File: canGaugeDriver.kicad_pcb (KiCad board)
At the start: 2 copper layers, 74.7 x 41.4 mm, 40 parts, among them J1 CANbed 1.0 Interface, J2 VIN INTERFACE, J3 BLUESMIRF, J4 1848710, U1 TPL7407LA, U2 TPL7407LA

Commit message: fixed headers
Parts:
- removed J3: BLUESMIRF, Connector_PinHeader_2.54mm:PinHeader_1x06_P2.54mm_Vertical
- moved J2 8.23 mm to (149.3, 76.9), turned to 0 degrees
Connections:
- J1 pad 10: /D0_RX -> /D8_SEATBELT
- J1 pad 11: /D1_TX -> /A0
- J1 pad 12: /D2_SRS -> /D9_FUEL
- J1 pad 13: /D3_SPEED -> /A1
- J1 pad 14: /D8_SEATBELT -> /D10_OIL
- J1 pad 15: /D9_FUEL -> /A2
- J1 pad 16: /D10_OIL -> /D11_TACH
- J1 pad 17: /D11_TACH -> /5V
- J1 pad 2: /D5_COOL -> /D0_RX
- J1 pad 3: /D6_ABS -> /D5_COOL
- J1 pad 4: /A3 -> /D1_TX
- J1 pad 5: /D12_ALT -> /D6_ABS
- J1 pad 6: /A0 -> /D2_SRS
- J1 pad 7: /A1 -> /A3
- J1 pad 8: /A2 -> /D3_SPEED
- J1 pad 9: /5V -> /D12_ALT
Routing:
- net /D0_RX: track 28.7 -> 0.00 mm, vias 1 -> 0
- net /D1_TX: track 24.6 -> 0.00 mm, vias 1 -> 0
- net /D11_TACH: track 51.7 -> 38.8 mm
- net /D5_COOL: track 32.7 -> 19.9 mm
- net /VIN: track 99.3 -> 87.9 mm
- net /5V: track 53.5 -> 44.9 mm
- net /D6_ABS: track 37.2 -> 29.6 mm
- net /D12_ALT: track 46.1 -> 38.8 mm
- net /A0: track 12.9 -> 6.20 mm
- net /A1: track 15.3 -> 9.22 mm
- net /A3: track 40.6 -> 35.7 mm
- net /D8_SEATBELT: track 54.0 -> 50.4 mm
- net /D9_FUEL: track 57.6 -> 54.0 mm
- net /A2: track 20.5 -> 17.0 mm
- net /D2_SRS: track 49.7 -> 47.3 mm
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
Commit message: replaced output connector
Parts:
- removed J4: 1848710, PHOENIX_1848710:PHOENIX_1848710
- added J3: 348260240, MOLEX_348260240:CONN_SD-34826-001_24_MOL, F.Cu at (162.6, 93.6)
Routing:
- net /AI3: track 72.1 -> 43.9 mm
- net /AI2: track 67.8 -> 43.9 mm
- net /AI1: track 74.4 -> 52.5 mm
- net /D12_OUT: track 33.7 -> 13.3 mm
- net /D8_OUT: track 36.5 -> 17.0 mm, vias 2 -> 1
- net /D6_OUT: track 32.0 -> 14.3 mm
- net /D5_OUT: track 28.8 -> 13.9 mm
- net /AI0: track 23.4 -> 8.53 mm
- net /D9_OUT: track 42.6 -> 29.6 mm
- net /D11_OUT: track 26.5 -> 14.1 mm
- net /D4_OUT: track 26.4 -> 14.7 mm
- net /D10_OUT: track 27.9 -> 17.5 mm
- net /D3_OUT: track 26.4 -> 17.1 mm
- net /D2_OUT: track 25.3 -> 17.7 mm

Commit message: progress
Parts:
- removed the ? at (130.0, 73.9)
- added J4: DB9'MEAL', canGaugeDriver:DB9-MEAL, F.Cu at (147.8, 80.9)
- C1, C2, C3, C4, C5, C6, JP1, JP2, R1, R10, R11, R12, R13, R14, R15, R16, R17, R18, R19, R2, R20, R21, R3, R4, R5, R6, R7, R8, R9: moved to B.Cu
- moved R16 31.0 mm to (133.1, 74.8), turned to 0 degrees
- moved JP1 30.3 mm to (128.0, 91.1), turned to 180 degrees
- moved R21 28.1 mm to (127.5, 98.2), turned to 90 degrees
- moved R17 27.8 mm to (133.1, 77.1), turned to 0 degrees
- moved R13 27.7 mm to (133.1, 71.0), turned to 0 degrees
- moved R15 24.9 mm to (133.1, 69.0), turned to 0 degrees
- moved R18 24.8 mm to (133.1, 79.1), turned to 0 degrees
- moved R14 22.3 mm to (133.1, 67.2), turned to 0 degrees
- moved R19 21.5 mm to (118.6, 81.7), turned to 0 degrees
- moved C5 20.7 mm to (131.3, 83.7), turned to 180 degrees
- moved R1 19.8 mm to (119.9, 91.1), turned to 180 degrees
- moved R12 19.8 mm to (133.1, 65.2), turned to 0 degrees
- moved R2 18.4 mm to (119.9, 88.3), turned to 0 degrees
- moved C6 15.8 mm to (129.8, 69.7), turned to 90 degrees
- moved U2 15.2 mm to (131.1, 79.6)
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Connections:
- J3 pad 1: unconnected-(J3-Pad1) -> /5V
- J3 pad 10: unconnected-(J3-Pad10) -> /VIN
- J3 pad 11: unconnected-(J3-Pad11) -> GND
- J3 pad 12: unconnected-(J3-Pad12) -> GND
- J3 pad 2: unconnected-(J3-Pad2) -> /5V
- J3 pad 24: unconnected-(J3-Pad24) -> GND
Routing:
- net /VIN: track 87.9 -> 0.00 mm, vias 5 -> 0
- net /D9_FUEL: track 54.0 -> 0.00 mm, vias 1 -> 0
- net /D10_OIL: track 52.6 -> 0.00 mm
- net /AI1: track 52.5 -> 0.00 mm, vias 2 -> 0
- net /D3_SPEED: track 51.6 -> 0.00 mm, vias 1 -> 0
- net /D8_SEATBELT: track 50.4 -> 0.00 mm, vias 1 -> 0
- net /D2_SRS: track 47.3 -> 0.00 mm, vias 1 -> 0
- net /5V: track 44.9 -> 0.00 mm, vias 2 -> 0
- net /AI2: track 43.9 -> 0.00 mm, vias 2 -> 0
- net /AI3: track 43.9 -> 0.00 mm, vias 1 -> 0
- net /AI0_SW: track 41.8 -> 0.00 mm
- net GND: track 40.8 -> 0.00 mm, vias 9 -> 0
- net /D11_TACH: track 38.8 -> 0.00 mm
- net /D12_ALT: track 38.8 -> 0.00 mm
- net /D4_CEL: track 36.7 -> 0.00 mm, vias 2 -> 0
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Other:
- board size 74.7 x 41.4 mm -> 80 x 41.4 mm

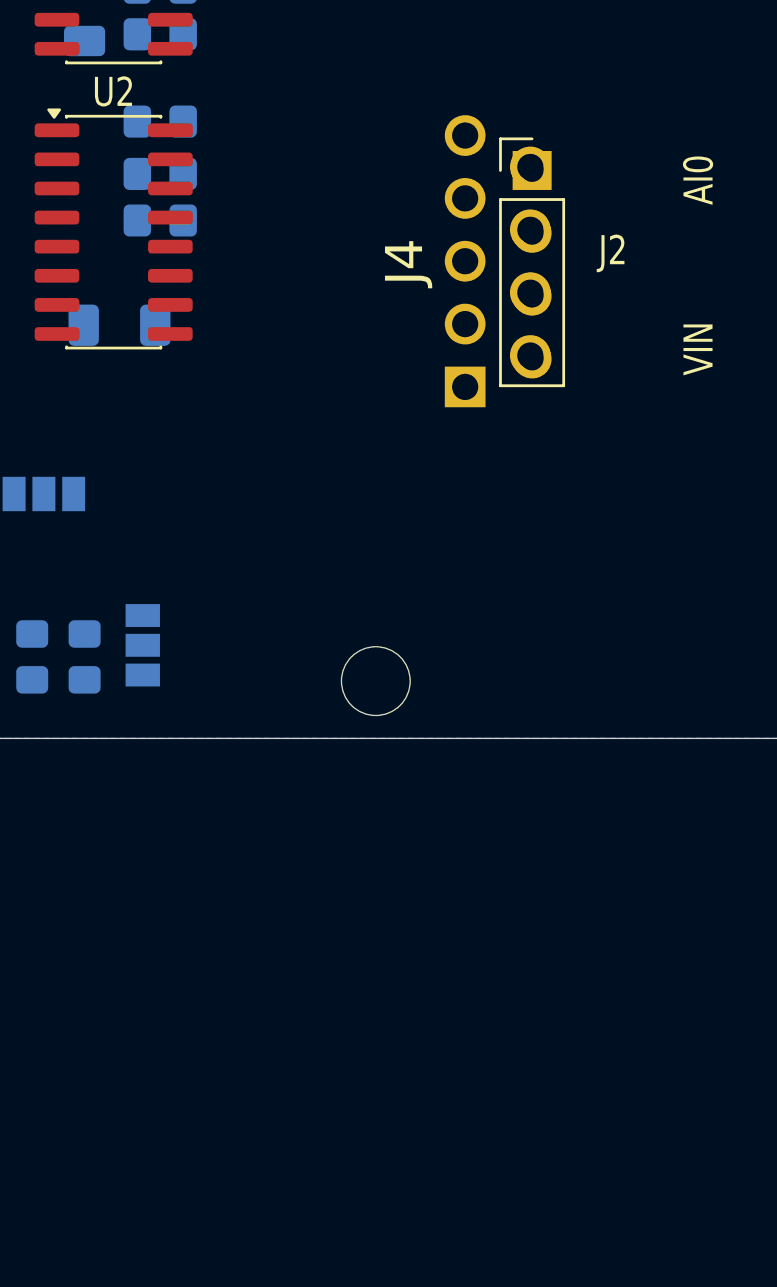
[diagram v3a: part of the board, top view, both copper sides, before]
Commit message: added external connector pinout
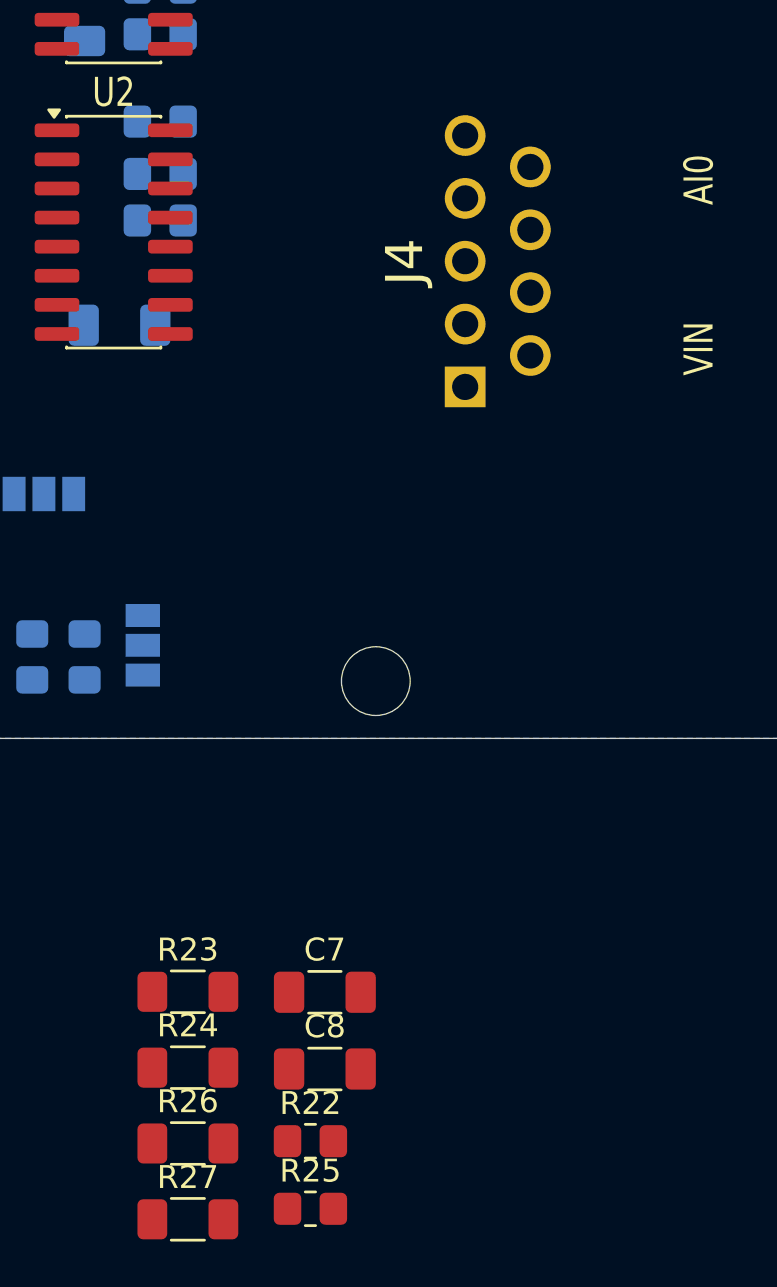
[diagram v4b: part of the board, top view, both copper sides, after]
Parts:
- removed J2: VIN INTERFACE, canGaugeDriver:VIN_Pins
- added C7: 1uF, Capacitor_SMD:C_1206_3216Metric_Pad1.33x1.80mm_HandSolder, F.Cu at (140.3, 112.8)
- added C8: 1uF, Capacitor_SMD:C_1206_3216Metric_Pad1.33x1.80mm_HandSolder, F.Cu at (140.3, 116.2)
- added R22: 10k, Resistor_SMD:R_0805_2012Metric_Pad1.20x1.40mm_HandSolder, F.Cu at (139.7, 119.3)
- added R23: 30.1k, Resistor_SMD:R_1206_3216Metric_Pad1.30x1.75mm_HandSolder, F.Cu at (134.3, 112.8)
- added R24: 9.76k, Resistor_SMD:R_1206_3216Metric_Pad1.30x1.75mm_HandSolder, F.Cu at (134.3, 116.1)
- added R25: 10k, Resistor_SMD:R_0805_2012Metric_Pad1.20x1.40mm_HandSolder, F.Cu at (139.7, 122.3)
- added R26: 30.1k, Resistor_SMD:R_1206_3216Metric_Pad1.30x1.75mm_HandSolder, F.Cu at (134.3, 119.4)
- added R27: 9.76k, Resistor_SMD:R_1206_3216Metric_Pad1.30x1.75mm_HandSolder, F.Cu at (134.3, 122.7)
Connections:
- J3 pad 13: unconnected-(J3-Pad13) -> /D2_OUT
- J3 pad 14: unconnected-(J3-Pad14) -> /D4_OUT
- J3 pad 15: unconnected-(J3-Pad15) -> /D6_OUT
- J3 pad 16: unconnected-(J3-Pad16) -> /AI0
- J3 pad 17: unconnected-(J3-Pad17) -> /AI1
- J3 pad 18: unconnected-(J3-Pad18) -> /AI2
- J3 pad 19: unconnected-(J3-Pad19) -> /AI3
- J3 pad 20: unconnected-(J3-Pad20) -> /D9_OUT
- J3 pad 21: unconnected-(J3-Pad21) -> /D11_OUT
- J3 pad 22: unconnected-(J3-Pad22) -> GND
- J3 pad 23: unconnected-(J3-Pad23) -> /CANL
- J3 pad 3: unconnected-(J3-Pad3) -> /D3_OUT
- J3 pad 4: unconnected-(J3-Pad4) -> /D5_OUT
- J3 pad 5: unconnected-(J3-Pad5) -> /D8_OUT
- J3 pad 6: unconnected-(J3-Pad6) -> /D10_OUT
- J3 pad 7: unconnected-(J3-Pad7) -> /D12_OUT
- J3 pad 8: unconnected-(J3-Pad8) -> /5V
- J3 pad 9: unconnected-(J3-Pad9) -> /CANH
- J4 pad 1: unconnected-(J4-Pad1) -> GND
- J4 pad 3: unconnected-(J4-Pad3) -> /CANH
- J4 pad 5: unconnected-(J4-Pad5) -> /CANL
- J4 pad 9: unconnected-(J4-Pad9) -> /VIN

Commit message: routed board
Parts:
- added R10: 10k, Resistor_SMD:R_0805_2012Metric_Pad1.20x1.40mm_HandSolder, B.Cu at (120.0, 95.1)
- added R11: 10k, Resistor_SMD:R_0805_2012Metric_Pad1.20x1.40mm_HandSolder, B.Cu at (120.0, 81.4)
- added R14: 10k, Resistor_SMD:R_0805_2012Metric_Pad1.20x1.40mm_HandSolder, B.Cu at (121.9, 69.5)
- added R2: 10k, Resistor_SMD:R_0805_2012Metric_Pad1.20x1.40mm_HandSolder, B.Cu at (121.9, 65.2)
- C1, C2: footprint Capacitor_SMD:C_1206_3216Metric_Pad1.33x1.80mm_HandSolder -> Capacitor_SMD:C_0805_2012Metric_Pad1.18x1.45mm_HandSolder
- C3: renamed from C7; footprint Capacitor_SMD:C_1206_3216Metric_Pad1.33x1.80mm_HandSolder -> Capacitor_SMD:C_0805_2012Metric_Pad1.18x1.45mm_HandSolder; moved to B.Cu
- C4: renamed from C3; footprint Capacitor_SMD:C_1206_3216Metric_Pad1.33x1.80mm_HandSolder -> Capacitor_SMD:C_0805_2012Metric_Pad1.18x1.45mm_HandSolder
- C5: renamed from C4; footprint Capacitor_SMD:C_1206_3216Metric_Pad1.33x1.80mm_HandSolder -> Capacitor_SMD:C_0805_2012Metric_Pad1.18x1.45mm_HandSolder
- C6: renamed from C8; footprint Capacitor_SMD:C_1206_3216Metric_Pad1.33x1.80mm_HandSolder -> Capacitor_SMD:C_0805_2012Metric_Pad1.18x1.45mm_HandSolder; moved to B.Cu
- C7: renamed from C6; footprint Capacitor_SMD:C_1206_3216Metric_Pad1.33x1.80mm_HandSolder -> Capacitor_SMD:C_0805_2012Metric_Pad1.18x1.45mm_HandSolder
- C8: renamed from C5; footprint Capacitor_SMD:C_1206_3216Metric_Pad1.33x1.80mm_HandSolder -> Capacitor_SMD:C_0805_2012Metric_Pad1.18x1.45mm_HandSolder
- JP2: moved to F.Cu
- R15: renamed from R25; moved to B.Cu
- R16: renamed from R5; footprint Resistor_SMD:R_1206_3216Metric_Pad1.30x1.75mm_HandSolder -> Resistor_SMD:R_0805_2012Metric_Pad1.20x1.40mm_HandSolder
- R17: renamed from R6; footprint Resistor_SMD:R_1206_3216Metric_Pad1.30x1.75mm_HandSolder -> Resistor_SMD:R_0805_2012Metric_Pad1.20x1.40mm_HandSolder
- R18: renamed from R7; footprint Resistor_SMD:R_1206_3216Metric_Pad1.30x1.75mm_HandSolder -> Resistor_SMD:R_0805_2012Metric_Pad1.20x1.40mm_HandSolder
- R19: renamed from R8; footprint Resistor_SMD:R_1206_3216Metric_Pad1.30x1.75mm_HandSolder -> Resistor_SMD:R_0805_2012Metric_Pad1.20x1.40mm_HandSolder
- R20: renamed from R26; footprint Resistor_SMD:R_1206_3216Metric_Pad1.30x1.75mm_HandSolder -> Resistor_SMD:R_0805_2012Metric_Pad1.20x1.40mm_HandSolder; moved to B.Cu
- R21: renamed from R27; footprint Resistor_SMD:R_1206_3216Metric_Pad1.30x1.75mm_HandSolder -> Resistor_SMD:R_0805_2012Metric_Pad1.20x1.40mm_HandSolder; moved to B.Cu
- R3: renamed from R22; moved to B.Cu
- R4: renamed from R1; footprint Resistor_SMD:R_1206_3216Metric_Pad1.30x1.75mm_HandSolder -> Resistor_SMD:R_0805_2012Metric_Pad1.20x1.40mm_HandSolder
- R5: renamed from R2; footprint Resistor_SMD:R_1206_3216Metric_Pad1.30x1.75mm_HandSolder -> Resistor_SMD:R_0805_2012Metric_Pad1.20x1.40mm_HandSolder
- R6: renamed from R3; footprint Resistor_SMD:R_1206_3216Metric_Pad1.30x1.75mm_HandSolder -> Resistor_SMD:R_0805_2012Metric_Pad1.20x1.40mm_HandSolder
- R7: renamed from R4; footprint Resistor_SMD:R_1206_3216Metric_Pad1.30x1.75mm_HandSolder -> Resistor_SMD:R_0805_2012Metric_Pad1.20x1.40mm_HandSolder
- R8: renamed from R23; value 30.1k -> 0; footprint Resistor_SMD:R_1206_3216Metric_Pad1.30x1.75mm_HandSolder -> Resistor_SMD:R_0805_2012Metric_Pad1.20x1.40mm_HandSolder; moved to B.Cu
- R9: renamed from R24; value 9.76k -> DNP; footprint Resistor_SMD:R_1206_3216Metric_Pad1.30x1.75mm_HandSolder -> Resistor_SMD:R_0805_2012Metric_Pad1.20x1.40mm_HandSolder; moved to B.Cu
- moved R3 57.7 mm to (119.6, 65.2), turned to -90 degrees
- moved R21 56.6 mm to (115.1, 69.5), turned to -90 degrees
- moved R15 56.5 mm to (119.6, 69.5), turned to 90 degrees
- moved C3 55.0 mm to (112.8, 65.2), turned to 90 degrees
- moved R9 54.5 mm to (115.1, 65.2), turned to 90 degrees
- moved C6 54.2 mm to (112.8, 69.5), turned to -90 degrees
- moved R20 52.7 mm to (117.3, 69.5), turned to 90 degrees
- moved R8 50.6 mm to (117.3, 65.2), turned to 90 degrees
- moved R12 18.4 mm to (122.3, 81.4), turned to -90 degrees
- moved R18 18.4 mm to (117.7, 81.4), turned to 90 degrees
- moved C5 15.3 mm to (113.2, 81.4), turned to -90 degrees
- moved R19 12.5 mm to (115.4, 81.4), turned to -90 degrees
- moved R1 12.0 mm to (127.4, 89.8)
- moved JP1 9.06 mm to (120.3, 86.4), turned to -90 degrees
- moved JP2 7.80 mm to (133.2, 89.9)
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- renumbered J4 to DB1, J3 to J2, R19 to R1, R20 to R12, R21 to R13, R10 to R22, R9 to R23, R11 to R24, R12 to R25, R14 to R26, R15 to R27, R13 to R28, R16 to R29, R17 to R30, R18 to R31
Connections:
- J2 pad 13: /D2_OUT -> /D0_IN
- J2 pad 14: /D4_OUT -> /D2_OUT
- J2 pad 15: /D6_OUT -> /D4_OUT
- J2 pad 20: /D9_OUT -> /D6_OUT
- J2 pad 21: /D11_OUT -> /D9_OUT
- J2 pad 22: GND -> /D11_OUT
- J2 pad 3: /D3_OUT -> /D1_IN
- J2 pad 4: /D5_OUT -> /D3_OUT
- J2 pad 5: /D8_OUT -> /D5_OUT
- J2 pad 6: /D10_OUT -> /D8_OUT
- J2 pad 7: /D12_OUT -> /D10_OUT
- J2 pad 8: /5V -> /D12_OUT
- R1 pad 2: /5V -> Net-(JP2-C)
- R12 pad 2: Net-(JP2-C) -> /VIN
- R15 pad 1: /AI2 -> /D1_IN
- R15 pad 2: /VIN -> /5V
- R20 pad 1: /AI2 -> /D1_IN
- R22 pad 1: /VIN -> /D2_OUT
- R22 pad 2: /D2_OUT -> /VIN
- R3 pad 1: /AI2 -> /D0_IN
- R3 pad 2: /VIN -> /5V
- R8 pad 1: /AI2 -> /D0_IN
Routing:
- net /5V: track 0.00 -> 147.8 mm, vias 0 -> 5
- net /VIN: track 0.00 -> 133.8 mm, vias 0 -> 7
- net /D0_IN: track 0.00 -> 85.6 mm
- net /D11_OUT: track 0.00 -> 80.5 mm, vias 0 -> 3
- net /D1_IN: track 0.00 -> 74.5 mm
- net /D2_OUT: track 0.00 -> 68.9 mm, vias 0 -> 2
- net /D4_OUT: track 0.00 -> 64.1 mm, vias 0 -> 2
- net /AI3: track 0.00 -> 64.0 mm, vias 0 -> 1
- net /AI1: track 0.00 -> 56.1 mm, vias 0 -> 3
- net /AI2: track 0.00 -> 54.9 mm, vias 0 -> 3
- net /AI0: track 0.00 -> 54.2 mm, vias 0 -> 1
- net /D12_OUT: track 0.00 -> 53.2 mm, vias 0 -> 1
- net /D5_OUT: track 0.00 -> 51.9 mm, vias 0 -> 2
- net /D10_OUT: track 0.00 -> 51.6 mm, vias 0 -> 3
- net /D3_OUT: track 0.00 -> 51.2 mm, vias 0 -> 2
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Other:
- board text added: "canGaugeDriver v2 V. Zaccardo"
- board text removed: "AI0"
- board text removed: "VIN"

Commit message: more routing
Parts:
- removed ? (x4): , 
- added H1: MountingHole, MountingHole:MountingHole_3mm, F.Cu at (104.1, 99.2)
- added H2: MountingHole, MountingHole:MountingHole_3mm, F.Cu at (104.1, 62.9)
- added H3: MountingHole, MountingHole:MountingHole_3mm, F.Cu at (142.5, 99.2)
- added H4: MountingHole, MountingHole:MountingHole_3mm, F.Cu at (142.5, 62.9)
- moved C7 2.79 mm to (127.8, 70.7)
- moved C8 2.79 mm to (129.3, 84.2)
- moved R22 2.79 mm to (131.1, 64.1)
- moved R25 2.79 mm to (131.1, 66.2)
- moved R26 2.79 mm to (131.1, 68.2)
- moved R27 2.79 mm to (131.1, 70.2)
- moved R28 2.79 mm to (131.1, 72.3)
- moved R29 2.79 mm to (131.1, 75.3)
- moved R30 2.79 mm to (131.1, 77.6)
- moved R31 2.79 mm to (131.1, 79.6)
- moved U1 2.79 mm to (129.0, 68.2)
- moved U2 2.79 mm to (129.0, 80.1)
- moved R23 1.78 mm to (137.2, 65.2)
- moved R24 1.78 mm to (135.1, 65.2)
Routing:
- net /VIN: track 133.8 -> 141.3 mm, vias 7 -> 6
- net /D3_OUT: track 51.2 -> 56.9 mm
- net /D10_OUT: track 51.6 -> 55.8 mm
- net /D5_OUT: track 51.9 -> 55.7 mm
- net /D11_OUT: track 80.5 -> 84.1 mm
- net /D12_OUT: track 53.2 -> 56.3 mm
- net /D5_COOL: track 42.2 -> 39.3 mm
- net /D9_FUEL: track 27.0 -> 24.2 mm
- net /D8_SEATBELT: track 26.4 -> 23.6 mm
- net /D6_ABS: track 31.6 -> 28.8 mm
- net /D3_SPEED: track 27.5 -> 24.7 mm
- net /D2_SRS: track 27.0 -> 24.2 mm
- net /D12_ALT: track 26.8 -> 24.0 mm
- net /D11_TACH: track 26.8 -> 24.0 mm
- net /D10_OIL: track 26.2 -> 23.4 mm
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
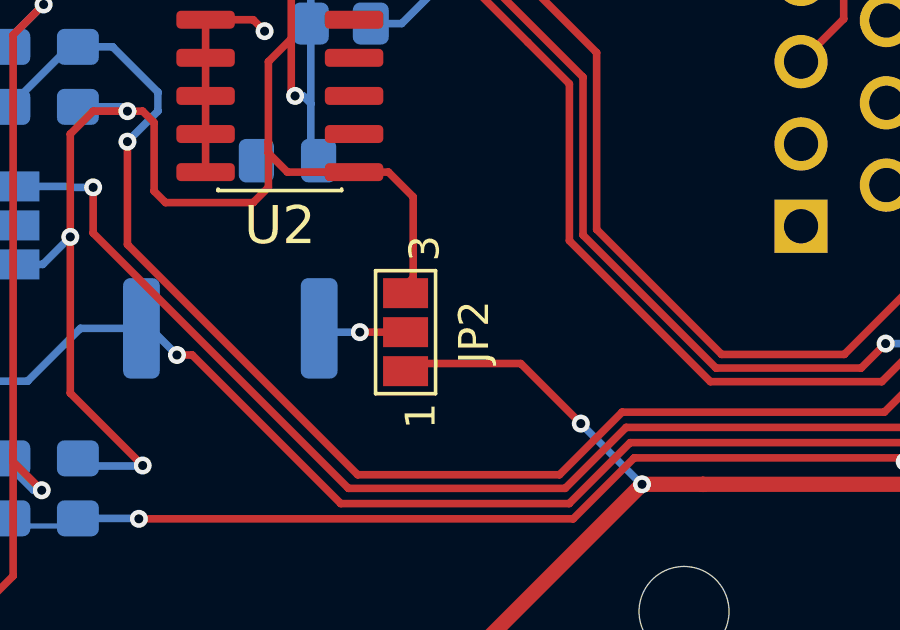
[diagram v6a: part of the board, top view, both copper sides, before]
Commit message: moved jumper to bottom of board
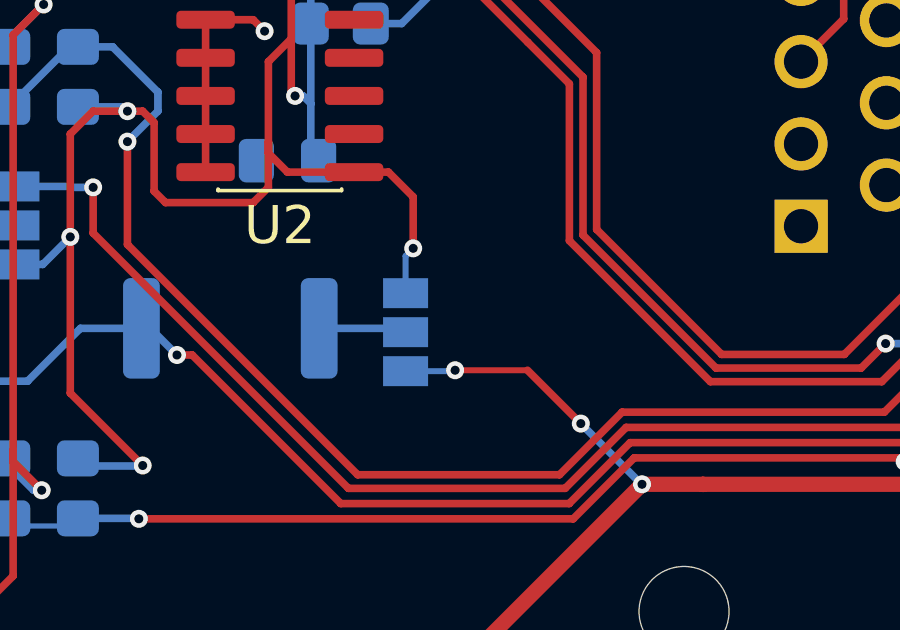
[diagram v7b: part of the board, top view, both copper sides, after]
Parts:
- JP2: moved to B.Cu
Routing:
- net /VIN: track 141.3 -> 141.5 mm, vias 6 -> 7
- net Net-(JP2-C): track 2.93 -> 3.11 mm, vias 1 -> 0
- net /5V: track 146.7 -> 146.6 mm, vias 5 -> 6

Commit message: minor cleanup
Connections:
- net /AI0 renamed /A0_IN
- net /AI1 renamed /A1_IN
- net /AI2 renamed /A2_IN
- net /AI3 renamed /A3_IN
- net /D0_RX renamed /D0
- net /D10_OIL renamed /D10
- net /D11_TACH renamed /D11
- net /D12_ALT renamed /D12
- net /D1_TX renamed /D1
- net /D2_SRS renamed /D2
- net /D3_SPEED renamed /D3
- net /D4_CEL renamed /D4
- net /D5_COOL renamed /D5
- net /D6_ABS renamed /D6
- net /D8_SEATBELT renamed /D8
- net /D9_FUEL renamed /D9
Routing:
- net GND: track 19.9 -> 15.6 mm, vias 3 -> 4
- net /CANL: track 27.4 -> 30.0 mm
- net /D11_OUT: track 84.1 -> 82.7 mm
